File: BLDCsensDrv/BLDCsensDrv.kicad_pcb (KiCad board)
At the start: 2 copper layers, 110 x 60 mm, 29 parts, among them IC1 DRV8300DIPWR, J1 Screw_Terminal_01x02, J2 Conn_01x08_Male, J3 Screw_Terminal_01x03, Q1 IRF540N, Q2 IRF540N, Q3 IRF540N, Q4 IRF540N, Q5 IRF540N, Q6 IRF540N, U1 LF50_TO252

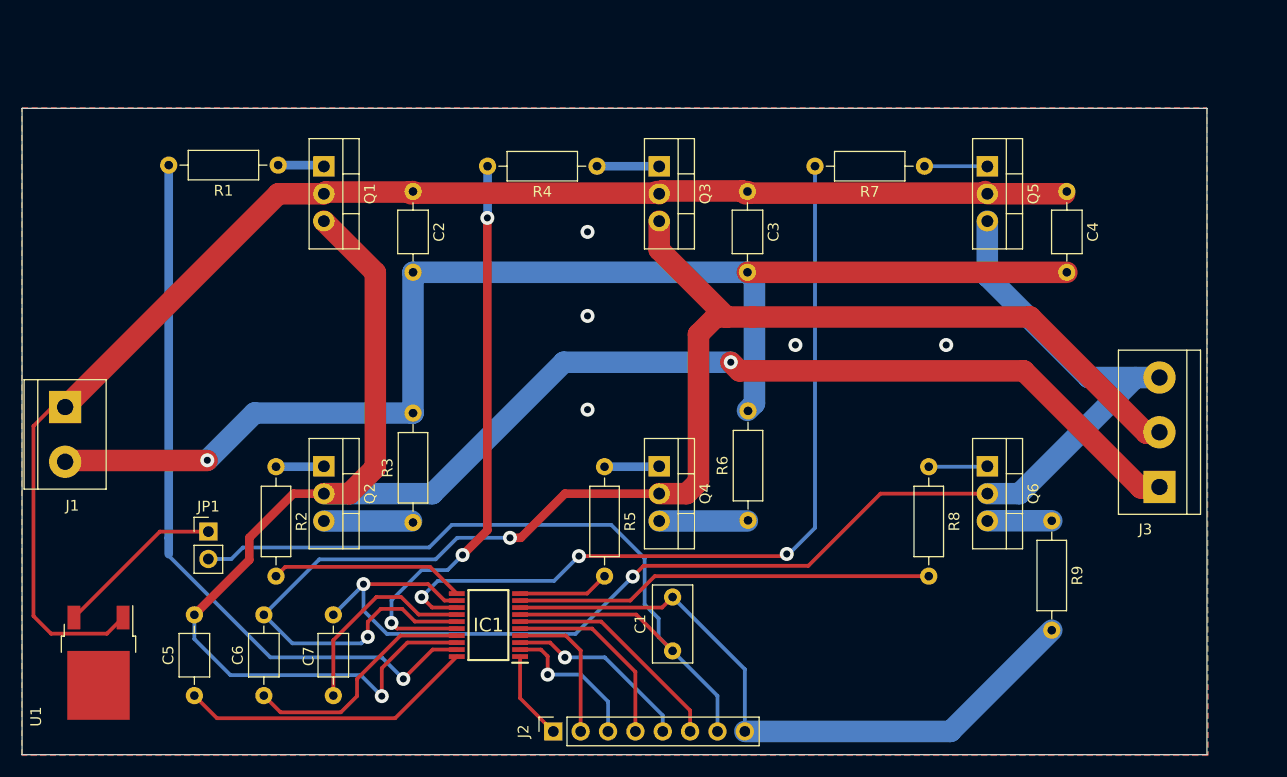
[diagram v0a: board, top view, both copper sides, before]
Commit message: 3-phase Trapezoidal Control hardware ready for prototype prod.
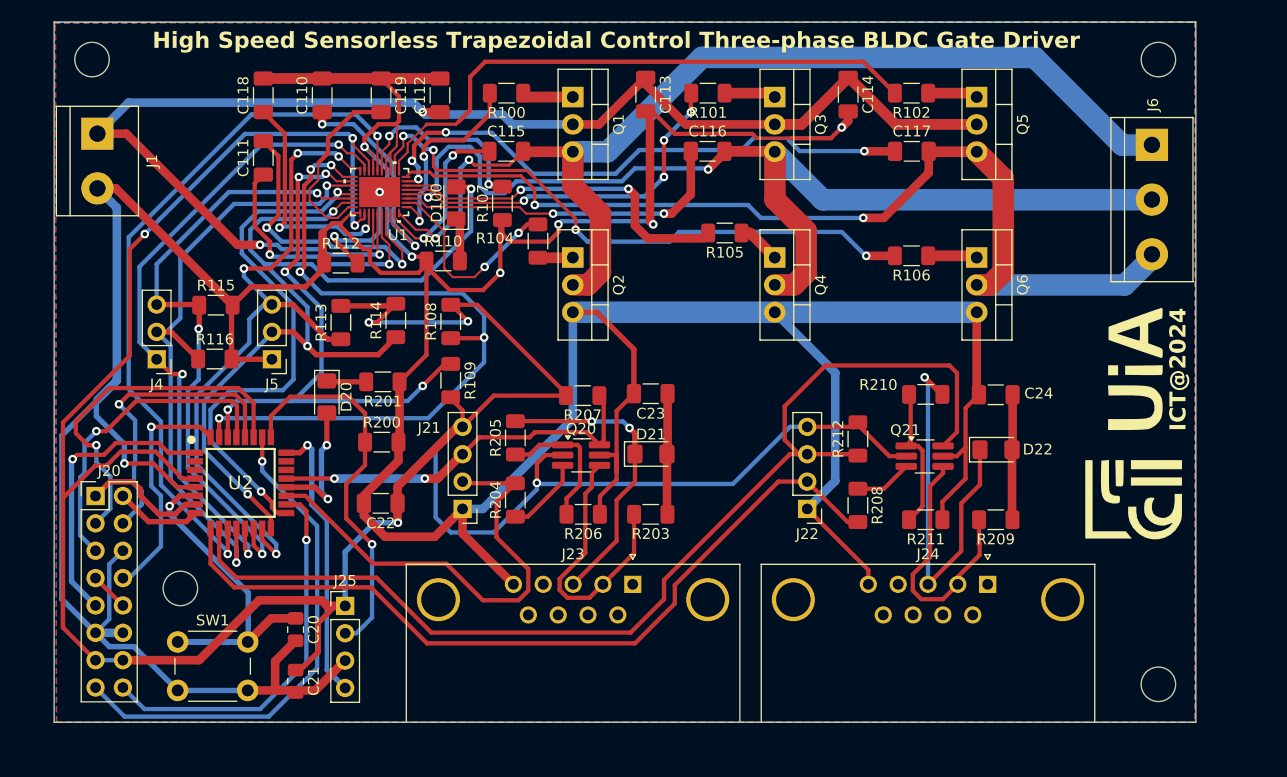
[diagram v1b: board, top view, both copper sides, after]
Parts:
- removed C1: 1000n, Capacitor_THT:C_Rect_L7.0mm_W3.5mm_P5.00mm
- removed C2, C3, C4, C5, C6, C7: 100n, Capacitor_THT:C_Axial_L3.8mm_D2.6mm_P7.50mm_Horizontal
- removed IC1: DRV8300DIPWR, SamacSys_Parts:SOP65P640X120-20N
- removed J2: Conn_01x08_Male, Connector_PinSocket_2.54mm:PinSocket_1x08_P2.54mm_Vertical
- removed J3: Screw_Terminal_01x03, TerminalBlock:TerminalBlock_bornier-3_P5.08mm
- removed JP1: Jumper_2_Open, Connector_PinHeader_2.54mm:PinHeader_1x02_P2.54mm_Vertical
- removed R1, R2, R4, R5, R7, R8: 15, Resistor_THT:R_Axial_DIN0207_L6.3mm_D2.5mm_P10.16mm_Horizontal
- removed R3, R6, R9: 0, Resistor_THT:R_Axial_DIN0207_L6.3mm_D2.5mm_P10.16mm_Horizontal
- added C110: 10u, Capacitor_SMD:C_1206_3216Metric_Pad1.33x1.80mm_HandSolder, F.Cu at (114.5, 64.5)
- added C111: 470n, Capacitor_SMD:C_1206_3216Metric_Pad1.33x1.80mm_HandSolder, F.Cu at (109.0, 70.3)
- added C112: 100n, Capacitor_SMD:C_1206_3216Metric_Pad1.33x1.80mm_HandSolder, F.Cu at (125.4, 64.5)
- added C113: 100n, Capacitor_SMD:C_1206_3216Metric_Pad1.33x1.80mm_HandSolder, F.Cu at (144.5, 64.5)
- added C114: 100n, Capacitor_SMD:C_1206_3216Metric_Pad1.33x1.80mm_HandSolder, F.Cu at (163.3, 64.5)
- added C115: 1µ, Capacitor_SMD:C_1206_3216Metric_Pad1.33x1.80mm_HandSolder, F.Cu at (131.6, 69.7)
- added C116: 1u, Capacitor_SMD:C_1206_3216Metric_Pad1.33x1.80mm_HandSolder, F.Cu at (150.2, 69.7)
- added C117: 1u, Capacitor_SMD:C_1206_3216Metric_Pad1.33x1.80mm_HandSolder, F.Cu at (169.2, 69.7)
- added C118: 2n, Capacitor_SMD:C_1206_3216Metric_Pad1.33x1.80mm_HandSolder, F.Cu at (109.0, 64.5)
- added C119: 1u, Capacitor_SMD:C_1206_3216Metric_Pad1.33x1.80mm_HandSolder, F.Cu at (119.9, 64.5)
- added C20: 100nF, Capacitor_SMD:C_0805_2012Metric_Pad1.18x1.45mm_HandSolder, F.Cu at (112.0, 114.1)
- added C21: 100nF, Capacitor_SMD:C_0805_2012Metric_Pad1.18x1.45mm_HandSolder, F.Cu at (112.0, 118.9)
- added C22: 10uF, Capacitor_SMD:C_1206_3216Metric_Pad1.33x1.80mm_HandSolder, F.Cu at (119.9, 102.4)
- added C23: 47uF, Capacitor_SMD:C_1206_3216Metric_Pad1.33x1.80mm_HandSolder, F.Cu at (145.0, 92.2)
- added C24: 47uF, Capacitor_SMD:C_1206_3216Metric_Pad1.33x1.80mm_HandSolder, F.Cu at (177.0, 92.3)
- added D100: LED, LED_SMD:LED_1206_3216Metric_Pad1.42x1.75mm_HandSolder, F.Cu at (126.9, 74.5)
- added D20: LED, LED_SMD:LED_1206_3216Metric_Pad1.42x1.75mm_HandSolder, F.Cu at (114.9, 92.5)
- added D21: 1N4148, Diode_SMD:D_1206_3216Metric_Pad1.42x1.75mm_HandSolder, F.Cu at (145.0, 97.8)
- added D22: 1N4148, Diode_SMD:D_1206_3216Metric_Pad1.42x1.75mm_HandSolder, F.Cu at (177.0, 97.4)
- added J20: Utility Pins, Connector_PinHeader_2.54mm:PinHeader_2x08_P2.54mm_Vertical, F.Cu at (93.4, 101.7)
- added J21: UART PORT#1, Connector_PinHeader_2.54mm:PinHeader_1x04_P2.54mm_Vertical, F.Cu at (127.5, 102.9)
- added J22: UART PORT#2, Connector_PinHeader_2.54mm:PinHeader_1x04_P2.54mm_Vertical, F.Cu at (159.5, 102.9)
- added J23: DB9_Female, Connector_Dsub:DSUB-9_Female_Horizontal_P2.77x2.84mm_EdgePinOffset9.90mm_Housed_MountingHolesOffset11.32mm, F.Cu at (143.3, 109.9)
- added J24: DB9_Female, Connector_Dsub:DSUB-9_Female_Horizontal_P2.77x2.84mm_EdgePinOffset9.90mm_Housed_MountingHolesOffset11.32mm, F.Cu at (176.2, 109.9)
- added J25: SWD, Connector_PinHeader_2.54mm:PinHeader_1x04_P2.54mm_Vertical, F.Cu at (116.6, 111.9)
- added J4: Ctrl-Port, Connector_PinHeader_2.54mm:PinHeader_1x03_P2.54mm_Vertical, F.Cu at (99.1, 89.0)
- added J5: Monitor, Connector_PinHeader_2.54mm:PinHeader_1x03_P2.54mm_Vertical, F.Cu at (109.8, 89.0)
- added J6: Screw_Terminal_01x03, TerminalBlock:TerminalBlock_bornier-3_P5.08mm, F.Cu at (191.5, 69.1)
- added Q20: FMB3946, Package_TO_SOT_SMD:TSOT-23-6_HandSoldering, F.Cu at (138.5, 97.9)
- added Q21: FMB3946, Package_TO_SOT_SMD:TSOT-23-6_HandSoldering, F.Cu at (170.4, 98.0)
- added R100: 15, Resistor_SMD:R_1206_3216Metric_Pad1.30x1.75mm_HandSolder, F.Cu at (131.6, 64.3)
- added R101: 15, Resistor_SMD:R_1206_3216Metric_Pad1.30x1.75mm_HandSolder, F.Cu at (150.3, 64.3)
- added R102: 15, Resistor_SMD:R_1206_3216Metric_Pad1.30x1.75mm_HandSolder, F.Cu at (169.2, 64.3)
- added R104: 15, Resistor_SMD:R_1206_3216Metric_Pad1.30x1.75mm_HandSolder, F.Cu at (134.5, 78.0)
- added R105: 15, Resistor_SMD:R_1206_3216Metric_Pad1.30x1.75mm_HandSolder, F.Cu at (151.8, 77.3)
- added R106: 15, Resistor_SMD:R_1206_3216Metric_Pad1.30x1.75mm_HandSolder, F.Cu at (169.2, 79.4)
- added R107: 0.1, Resistor_SMD:R_1206_3216Metric_Pad1.30x1.75mm_HandSolder, F.Cu at (131.2, 74.5)
- added R108: 5.1k, Resistor_SMD:R_1206_3216Metric_Pad1.30x1.75mm_HandSolder, F.Cu at (126.4, 85.5)
- added R109: 5.1k, Resistor_SMD:R_1206_3216Metric_Pad1.30x1.75mm_HandSolder, F.Cu at (126.4, 91.0)
- added R110: 1k, Resistor_SMD:R_1206_3216Metric_Pad1.30x1.75mm_HandSolder, F.Cu at (125.7, 79.9)
- added R112: 0, Resistor_SMD:R_1206_3216Metric_Pad1.30x1.75mm_HandSolder, F.Cu at (116.2, 80.1)
- added R113: 5.1k, Resistor_SMD:R_1206_3216Metric_Pad1.30x1.75mm_HandSolder, F.Cu at (116.2, 85.6)
- added R114: 5.1k, Resistor_SMD:R_1206_3216Metric_Pad1.30x1.75mm_HandSolder, F.Cu at (121.3, 85.4)
- added R115: 10k, Resistor_SMD:R_1206_3216Metric_Pad1.30x1.75mm_HandSolder, F.Cu at (104.6, 84.0)
- added R116: 10k, Resistor_SMD:R_1206_3216Metric_Pad1.30x1.75mm_HandSolder, F.Cu at (104.5, 89.0)
- added R200: 10k, Resistor_SMD:R_1206_3216Metric_Pad1.30x1.75mm_HandSolder, F.Cu at (120.0, 96.7)
- added R201: 1k, Resistor_SMD:R_1206_3216Metric_Pad1.30x1.75mm_HandSolder, F.Cu at (120.1, 91.1)
- added R203: 10k, Resistor_SMD:R_1206_3216Metric_Pad1.30x1.75mm_HandSolder, F.Cu at (145.0, 103.4)
- added R204: 10k, Resistor_SMD:R_1206_3216Metric_Pad1.30x1.75mm_HandSolder, F.Cu at (132.4, 102.1)
- added R205: 10k, Resistor_SMD:R_1206_3216Metric_Pad1.30x1.75mm_HandSolder, F.Cu at (132.4, 96.3)
- added R206: 10k, Resistor_SMD:R_1206_3216Metric_Pad1.30x1.75mm_HandSolder, F.Cu at (138.7, 103.4)
- added R207: 10k, Resistor_SMD:R_1206_3216Metric_Pad1.30x1.75mm_HandSolder, F.Cu at (138.7, 92.4)
- added R208: 10k, Resistor_SMD:R_1206_3216Metric_Pad1.30x1.75mm_HandSolder, F.Cu at (164.2, 102.6)
- added R209: 10k, Resistor_SMD:R_1206_3216Metric_Pad1.30x1.75mm_HandSolder, F.Cu at (177.0, 103.9)
- added R210: 10k, Resistor_SMD:R_1206_3216Metric_Pad1.30x1.75mm_HandSolder, F.Cu at (170.5, 92.3)
- added R211: 10k, Resistor_SMD:R_1206_3216Metric_Pad1.30x1.75mm_HandSolder, F.Cu at (170.5, 103.9)
- added R212: 10k, Resistor_SMD:R_1206_3216Metric_Pad1.30x1.75mm_HandSolder, F.Cu at (164.2, 96.4)
- added REF**: MountingHole_3.2mm_M3, MountingHole:MountingHole_3.2mm_M3, F.Cu at (93.1, 61.2)
- added REF**: MountingHole_3.2mm_M3, MountingHole:MountingHole_3.2mm_M3, F.Cu at (101.3, 110.3)
- added REF**: MountingHole_3.2mm_M3, MountingHole:MountingHole_3.2mm_M3, F.Cu at (192.1, 119.2)
- added REF**: MountingHole_3.2mm_M3, MountingHole:MountingHole_3.2mm_M3, F.Cu at (192.1, 61.2)
- added SW1: RESET, Button_Switch_THT:SW_PUSH_6mm_H5mm, F.Cu at (101.0, 115.3)
- added U2: STM32G030K6T6, BLDCsens:QFP80P900X900X160-32N, F.Cu at (106.9, 100.5)
- U1: value LF50_TO252 -> MCT8329A1IREER; footprint Package_TO_SOT_SMD:TO-252-2 -> BLDCsens:WQFN36_REE_TEX
- moved G*** 88.8 mm to (189.8, 95.0), turned to 90 degrees
- moved U1 50.9 mm to (119.8, 73.5), turned to 90 degrees
- moved Q2 30.2 mm to (137.7, 79.6)
- moved J1 25.6 mm to (93.6, 68.1)
- moved Q1 24.0 mm to (137.7, 64.7)
- moved Q4 22.2 mm to (156.5, 79.6)
- moved Q6 19.4 mm to (175.2, 79.6)
- moved Q3 12.5 mm to (156.5, 64.7)
- moved Q5 6.51 mm to (175.2, 64.7)
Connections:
- J1 pad 1: +BATT -> Net-(J1-Pin_1)
- J1 pad 2: GNDREF -> AGND
- Q1 pad 2: +BATT -> Net-(J1-Pin_1)
- Q1 pad 3: Net-(C5-Pad2) -> Net-(J6-Pin_1)
- Q2 pad 2: Net-(C5-Pad2) -> Net-(J6-Pin_1)
- Q2 pad 3: Net-(Q2-Pad3) -> AGND
- Q3 pad 2: +BATT -> Net-(J1-Pin_1)
- Q3 pad 3: Net-(C6-Pad2) -> Net-(J6-Pin_2)
- Q4 pad 2: Net-(C6-Pad2) -> Net-(J6-Pin_2)
- Q4 pad 3: Net-(Q4-Pad3) -> AGND
- Q5 pad 2: +BATT -> Net-(J1-Pin_1)
- Q5 pad 3: Net-(C7-Pad2) -> Net-(J6-Pin_3)
- Q6 pad 2: Net-(C7-Pad2) -> Net-(J6-Pin_3)
- Q6 pad 3: Net-(Q6-Pad3) -> AGND
- U1 pad 1: +BATT -> AGND
- U1 pad 2: GNDREF -> AVDD
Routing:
- net AGND: track 0.00 -> 463.4 mm, vias 0 -> 7
- net AVDD: track 0.00 -> 277.7 mm, vias 0 -> 7
- net GNDREF: track 183.6 -> 0.00 mm, vias 6 -> 0
- net Net-(C5-Pad2): track 168.3 -> 0.00 mm, vias 2 -> 0
- net Net-(C6-Pad2): track 140.1 -> 0.00 mm, vias 2 -> 0
- net +BATT: track 133.2 -> 0.00 mm
- net Net-(C7-Pad2): track 127.8 -> 0.00 mm, vias 2 -> 0
- net Net-(J1-Pin_1): track 0.00 -> 127.6 mm, vias 0 -> 3
- net USART2_RX: track 0.00 -> 103.9 mm
- net Net-(J6-Pin_1): track 0.00 -> 99.4 mm, vias 0 -> 2
- net Net-(J6-Pin_2): track 0.00 -> 95.8 mm, vias 0 -> 2
- net Net-(J6-Pin_3): track 0.00 -> 92.5 mm, vias 0 -> 2
- net NFAULT: track 0.00 -> 89.0 mm, vias 0 -> 4
- net Net-(C1-Pad1): track 77.5 -> 0.00 mm
- net Net-(IC1-Pad13): track 76.4 -> 0.00 mm, vias 3 -> 0
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- added copper zone on B.Cu, net AGND
- added copper zone on F.Cu, net AGND
- removed copper zone on B.Cu, net GNDREF
- removed copper zone on F.Cu, net GNDREF
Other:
- board size 110 x 60 mm -> 106 x 65 mm
- board text added: "High Speed Sensorless Trapezoidal Control Three-phase BLDC Gate Driver"
- board text added: "ICT@2024"
